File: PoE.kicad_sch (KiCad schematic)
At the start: 41 parts, among them J1001 8P8C_LED_Shielded_x2, J1002 8P8C_LED_Shielded_x2, U1001 7490220122, U1002 TCMT1107

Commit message: Still needs a lot of work
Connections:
- net POE0 renamed POE0_P
- net POE1 renamed POE0_N
- net POE2 renamed POE1_P
- net POE3 renamed POE1_N
- net POE4 renamed POE2_P
- net POE5 renamed POE2_N
- net POE6 renamed POE3_P
- net POE7 renamed POE3_N
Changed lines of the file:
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@@
 		)
 	)
-	(label "POE7"
+	(label "POE3_N"
 		(at 59.69 62.23 0)
 		(fields_autoplaced yes)
@@
 		)
 	)
-	(label "POE2"
+	(label "POE1_P"
 		(at 59.69 49.53 0)
 		(fields_autoplaced yes)
@@
 		)
 	)
-	(label "POE3"
+	(label "POE1_N"
 		(at 110.49 45.72 0)
 		(fields_autoplaced yes)
@@
 		)
 	)
-	(label "POE7"
+	(label "POE3_N"
 		(at 110.49 55.88 0)
 		(fields_autoplaced yes)
@@
 		)
 	)
-	(label "POE3"
+	(label "POE1_N"
 		(at 59.69 52.07 0)
 		(fields_autoplaced yes)
@@
 		)
 	)
-	(label "POE1"
+	(label "POE0_N"
 		(at 110.49 33.02 0)
 		(fields_autoplaced yes)
@@
 		)
 	)
-	(label "POE4"
+	(label "POE2_P"
 		(at 110.49 48.26 0)
 		(fields_autoplaced yes)
@@
 		)
 	)
-	(label "POE6"
+	(label "POE3_P"
 		(at 59.69 59.69 0)
 		(fields_autoplaced yes)
@@
 		)
 	)
-	(label "POE1"
+	(label "POE0_N"
 		(at 59.69 46.99 0)
 		(fields_autoplaced yes)
@@
 		)
 	)
-	(label "POE5"
+	(label "POE2_N"
 		(at 110.49 40.64 0)
 		(fields_autoplaced yes)
@@
 		)
 	)
-	(label "POE0"
+	(label "POE0_P"
 		(at 59.69 44.45 0)
 		(fields_autoplaced yes)
@@
 		)
 	)
-	(label "POE6"
+	(label "POE3_P"
 		(at 110.49 53.34 0)
 		(fields_autoplaced yes)
@@
 		)
 	)
-	(label "POE5"
+	(label "POE2_N"
 		(at 59.69 57.15 0)
 		(fields_autoplaced yes)
@@
 		)
 	)
-	(label "POE2"
+	(label "POE1_P"
 		(at 110.49 38.1 0)
 		(fields_autoplaced yes)
@@
 		)
 	)
-	(label "POE0"
+	(label "POE0_P"
 		(at 110.49 30.48 0)
 		(fields_autoplaced yes)
@@
 		)
 	)
-	(label "POE4"
+	(label "POE2_P"
 		(at 59.69 54.61 0)
 		(fields_autoplaced yes)
@@
 			)
 		)
+	)
+	(netclass_flag ""
+		(length 2.54)
+		(shape round)
+		(at 52.07 52.07 0)
+		(fields_autoplaced yes)
+		(effects
+			(font
+				(size 1.27 1.27)
+			)
+			(justify left bottom)
+		)
+		(property "Netclass" "Diff"
+			(at 52.7685 49.53 0)
+			(effects
+				(font
+					(size 1.27 1.27)
+					(italic yes)
+				)
+				(justify left)
+			)
+		)
+	)
+	(netclass_flag ""
+		(length 2.54)
+		(shape round)
+		(at 53.34 54.61 0)
+		(fields_autoplaced yes)
+		(effects
+			(font
+				(size 1.27 1.27)
+			)
+			(justify left bottom)
+		)
+		(property "Netclass" "Diff"
+			(at 54.0385 52.07 0)
+			(effects
+				(font
+					(size 1.27 1.27)
+					(italic yes)
+				)
+				(justify left)
+			)
+		)
+	)
+	(netclass_flag ""
+		(length 2.54)
+		(shape round)
+		(at 54.61 62.23 0)
+		(fields_autoplaced yes)
+		(effects
+			(font
+				(size 1.27 1.27)
+			)
+			(justify left bottom)
+		)
+		(property "Netclass" "Diff"
+			(at 55.3085 59.69 0)
+			(effects
+				(font
+					(size 1.27 1.27)
+					(italic yes)
+				)
+				(justify left)
+			)
+		)
+	)
+	(netclass_flag ""
+		(length 2.54)
+		(shape round)
+		(at 55.88 57.15 0)
+		(fields_autoplaced yes)
+		(effects
+			(font
+				(size 1.27 1.27)
+			)
+			(justify left bottom)
+		)
+		(property "Netclass" "Diff"
+			(at 56.5785 54.61 0)
+			(effects
+				(font
+					(size 1.27 1.27)
+					(italic yes)
+				)
+				(justify left)
+			)
+		)
+	)
+	(netclass_flag ""
+		(length 2.54)
+		(shape round)
+		(at 54.61 46.99 0)
+		(fields_autoplaced yes)
+		(effects
+			(font
+				(size 1.27 1.27)
+			)
+			(justify left bottom)
+		)
+		(property "Netclass" "Diff"
+			(at 55.3085 44.45 0)
+			(effects
+				(font
+					(size 1.27 1.27)
+					(italic yes)
+				)
+				(justify left)
+			)
+		)
+	)
+	(netclass_flag ""
+		(length 2.54)
+		(shape round)
+		(at 53.34 44.45 0)
+		(fields_autoplaced yes)
+		(effects
+			(font
+				(size 1.27 1.27)
+			)
+			(justify left bottom)
+		)
+		(property "Netclass" "Diff"
+			(at 54.0385 41.91 0)
+			(effects
+				(font
+					(size 1.27 1.27)
+					(italic yes)
+				)
+				(justify left)
+			)
+		)
+	)
+	(netclass_flag ""
+		(length 2.54)
+		(shape round)
+		(at 52.07 59.69 0)
+		(fields_autoplaced yes)
+		(effects
+			(font
+				(size 1.27 1.27)
+			)
+			(justify left bottom)
+		)
+		(property "Netclass" "Diff"
+			(at 52.7685 57.15 0)
+			(effects
+				(font
+					(size 1.27 1.27)
+					(italic yes)
+				)
+				(justify left)
+			)
+		)
+	)
+	(netclass_flag ""
+		(length 2.54)
+		(shape round)
+		(at 55.88 49.53 0)
+		(fields_autoplaced yes)
+		(effects
+			(font
+				(size 1.27 1.27)
+			)
+			(justify left bottom)
+		)
+		(property "Netclass" "Diff"
+			(at 56.5785 46.99 0)
+			(effects
+				(font
+					(size 1.27 1.27)
+					(italic yes)
+				)
+				(justify left)
+			)
+		)

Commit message: Added routing
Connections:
- net VDD_PRIME: now reaches C1007.1, D1001.1 (K), D1002.1 (K), D1003.1 (K), D1004.1 (K), FB1001.2
- net VSS_PRIME: now reaches C1007.2, D1006.2 (A), D1007.2 (A), D1008.2 (A), D1009.2 (A), FB1002.2
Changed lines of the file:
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@@
+		)
+	)
+	(label "VSS_PRIME"
+		(at 210.82 114.3 0)
+		(fields_autoplaced yes)
+		(effects
+			(font
+				(size 1.27 1.27)
+			)
+			(justify left bottom)
 		)
 	)
@@
 		(fields_autoplaced yes)
 		(effects
+			(font
+				(size 1.27 1.27)
+			)
+			(justify left bottom)
+		)
+	)
+	(label "VDD_PRIME"
+		(at 210.82 82.55 0)
+		(fields_autoplaced yes)
+		(effects

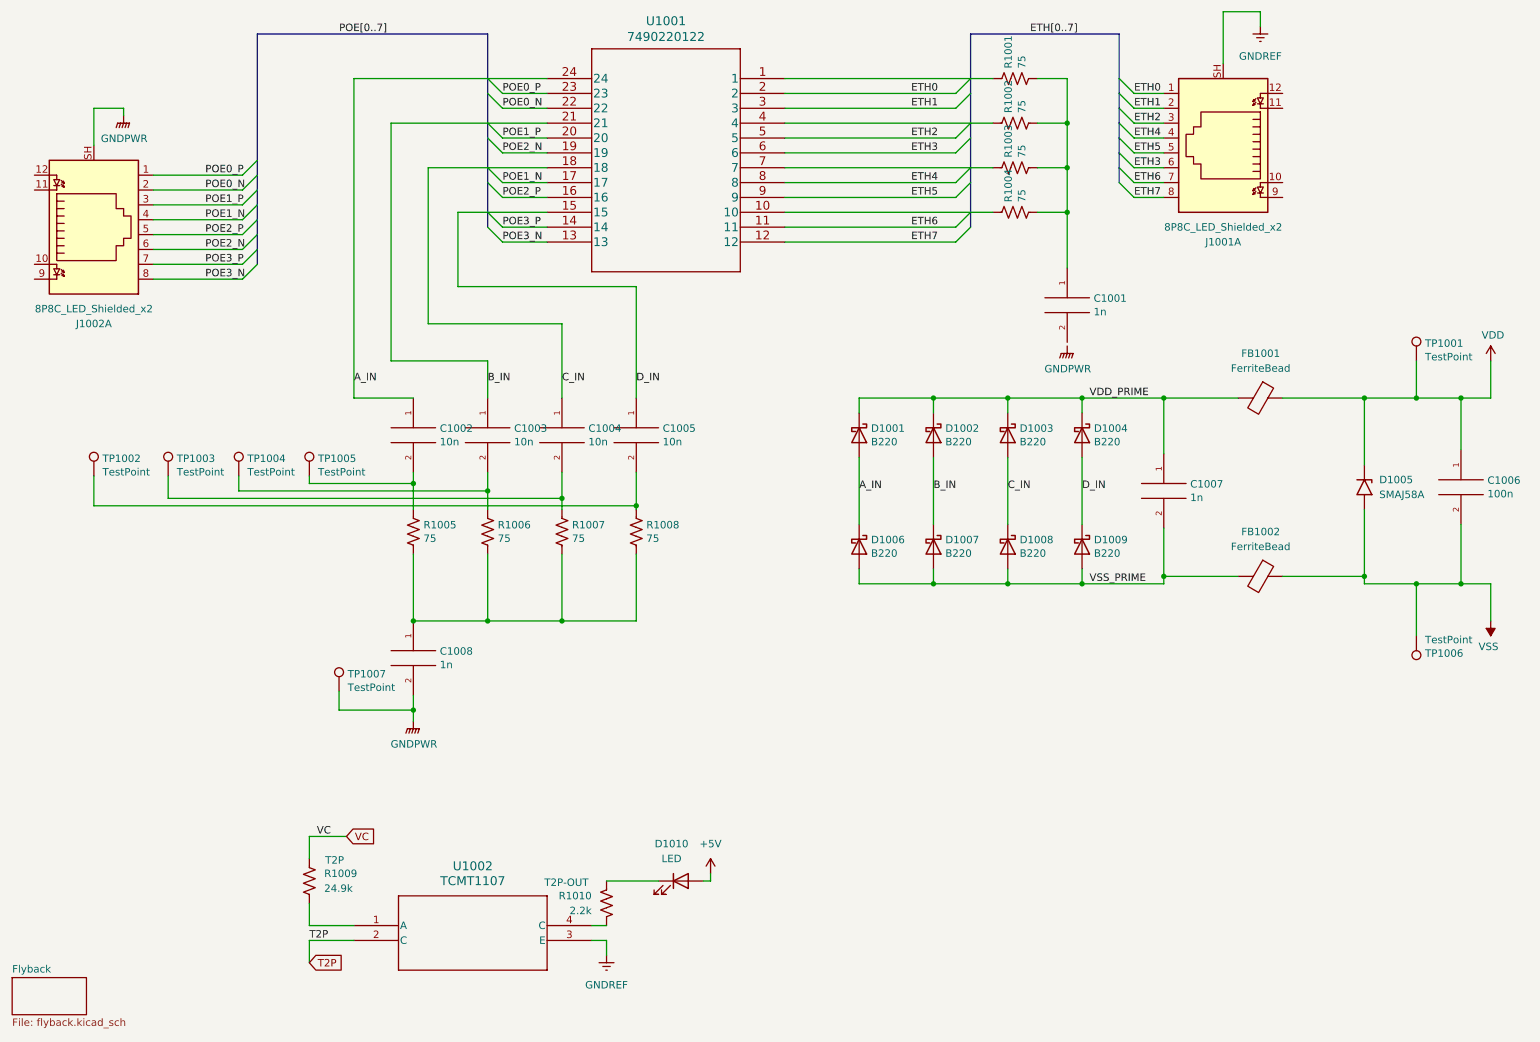
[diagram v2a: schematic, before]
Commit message: Changed main FET
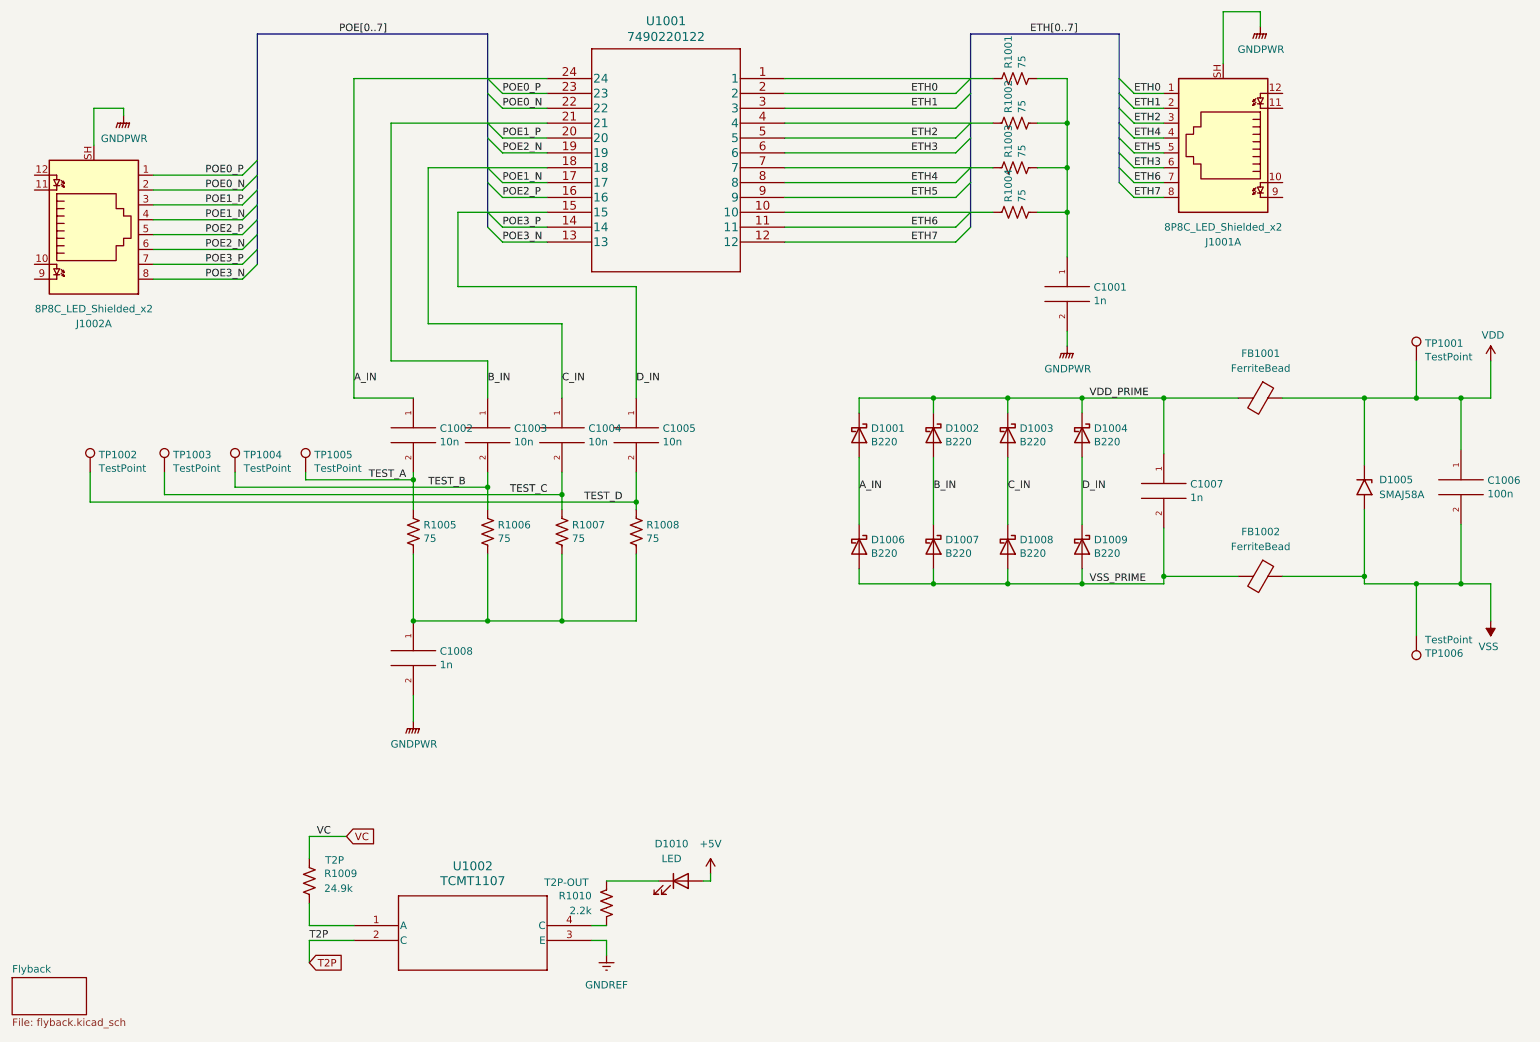
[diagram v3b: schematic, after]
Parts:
- removed TP1007: TestPoint, SparkFun-Connector:TestPoint-1.0mm, symbol Connector:TestPoint
- D1010: footprint LED_SMD:LED_0402_1005Metric -> LED_SMD:LED_0805_2012Metric
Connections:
- net GNDPWR: now also C1001.2, J1001.SH
- net GNDREF: no longer J1001.SH
- net TEST_A: now reaches C1002.2, R1005.1, TP1005.1
- net TEST_B: now reaches C1003.2, R1006.1, TP1004.1
- net TEST_C: now reaches C1004.2, R1007.1, TP1003.1
- net TEST_D: now reaches C1005.2, R1008.1, TP1002.1
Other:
- moved on the sheet: C1001, TP1002, TP1003, TP1004, TP1005

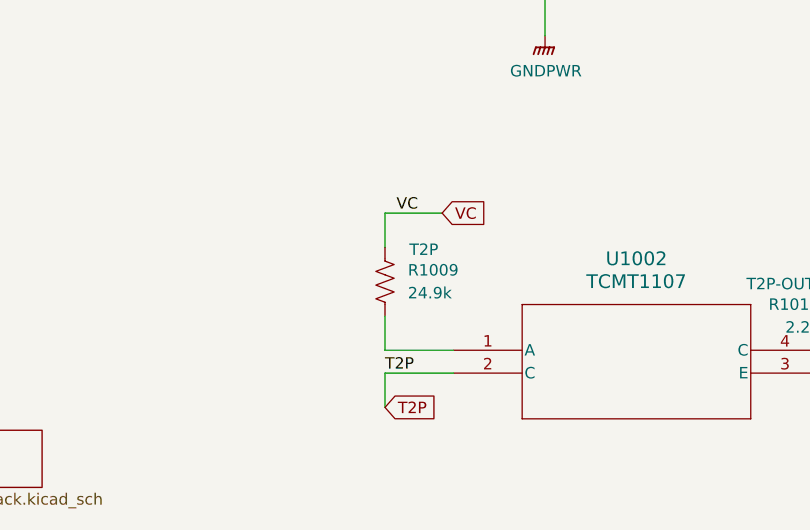
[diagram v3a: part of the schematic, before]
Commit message: Added more routing
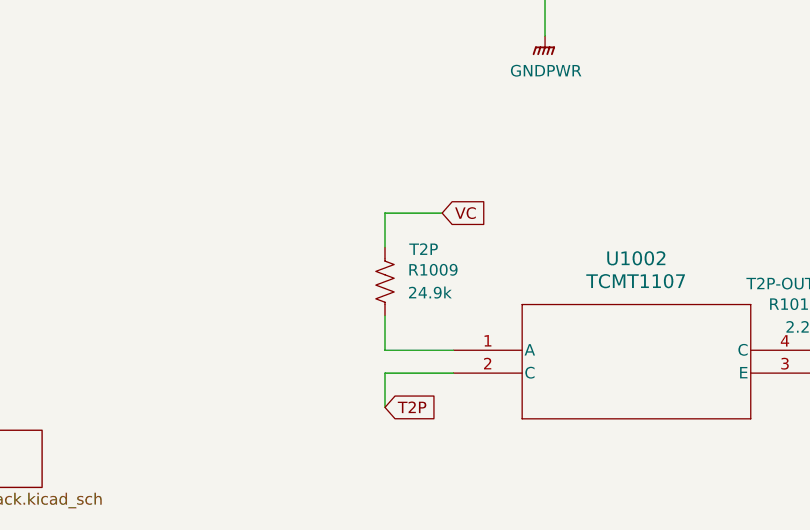
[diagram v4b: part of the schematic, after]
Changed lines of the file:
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@@
-		)
-	)
-	(label "VC"
-		(at 78.74 157.48 0)
-		(fields_autoplaced yes)
-		(effects
-			(font
-				(size 1.27 1.27)
-			)
-			(justify left bottom)
 		)
 	)
@@
 		(fields_autoplaced yes)
 		(effects
-			(font
-				(size 1.27 1.27)
-			)
-			(justify left bottom)
-		)
-	)
-	(label "T2P"
-		(at 77.47 175.26 0)
-		(fields_autoplaced yes)
-		(effects

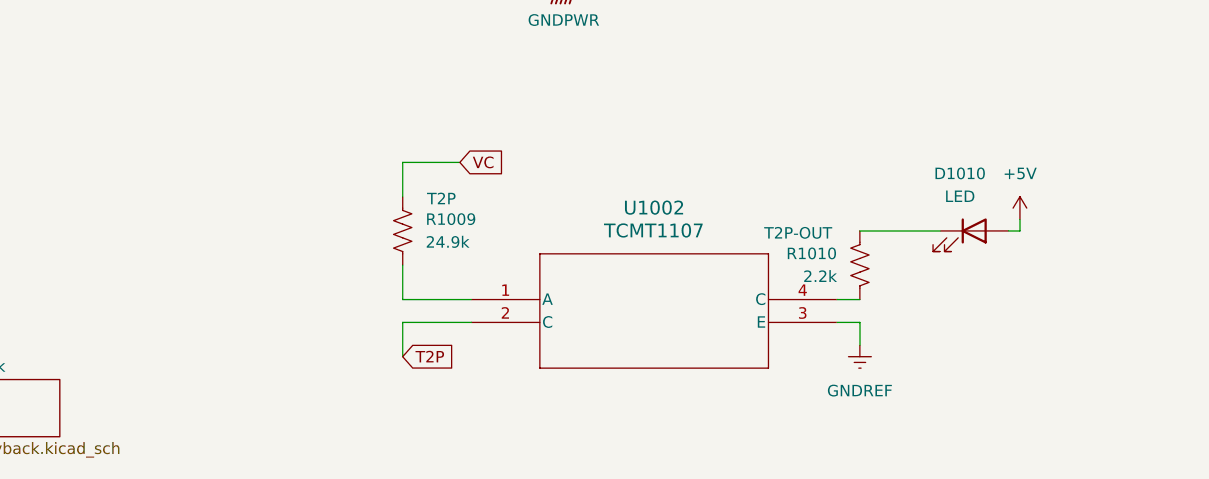
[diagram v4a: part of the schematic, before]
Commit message: Added buck
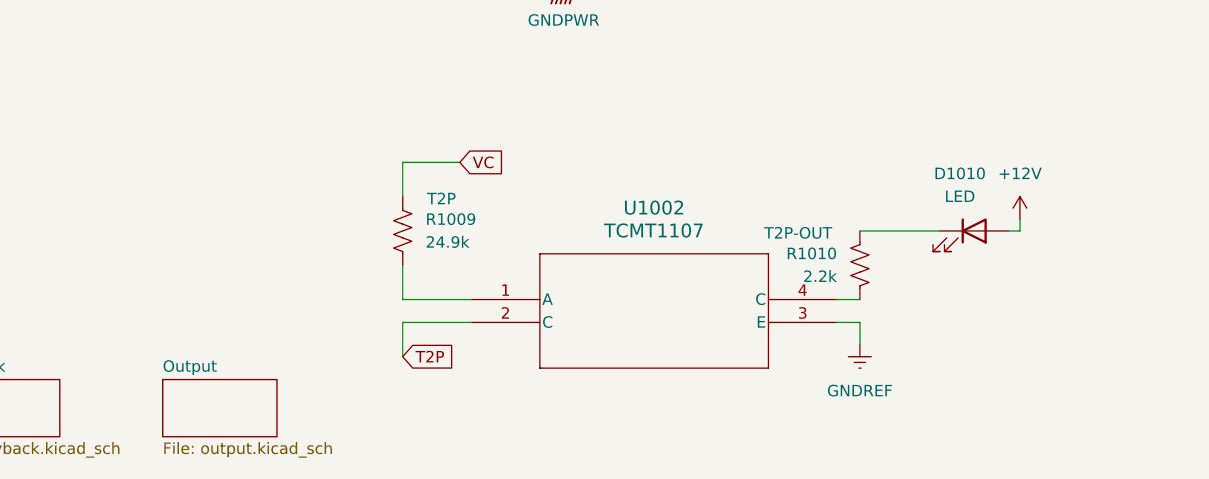
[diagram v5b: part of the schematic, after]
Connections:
- net +5V renamed +12V
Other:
- added sheet Output (output.kicad_sch)
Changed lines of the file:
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@@
+	)
+	(symbol
+		(lib_id "power:+12V")
+		(at 146.05 163.83 0)
+		(unit 1)
+		(exclude_from_sim no)
+		(in_bom yes)
+		(on_board yes)
+		(dnp no)
+		(fields_autoplaced yes)
+		(property "Reference" "#PWR014"
+			(at 146.05 167.64 0)
+			(effects
+				(font
+					(size 1.27 1.27)
+				)
+				(hide yes)
+			)
+		)
+		(property "Value" "+12V"
+			(at 146.05 158.75 0)
+			(effects
+				(font
+					(size 1.27 1.27)
+				)
+			)
+		)
+		(property "Footprint" ""
+			(at 146.05 163.83 0)
+			(effects
+				(font
+					(size 1.27 1.27)
+				)
+				(hide yes)
+			)
+		)
+		(property "Datasheet" ""
+			(at 146.05 163.83 0)
+			(effects
+				(font
+					(size 1.27 1.27)
+				)
+				(hide yes)
+			)
+		)
+		(property "Description" "Power symbol creates a global label with name \"+12V\""
+			(at 146.05 163.83 0)
+			(effects
+				(font
+					(size 1.27 1.27)
+				)
+				(hide yes)
+			)
+		)
+		(pin "1"
+		)
+		(instances
+			(project "PoE"
+				(path "/e8d70991-5081-4afb-b8c3-5ce9f62355e0"
+					(reference "#PWR014")
+					(unit 1)
+				)
+			)
+		)
 	)
 	(symbol
@@
 				(path "/e8d70991-5081-4afb-b8c3-5ce9f62355e0"
 					(reference "D1005")
-					(unit 1)
-				)
-			)
-		)
-	)
-	(symbol
-		(lib_id "power:+5V")
-		(at 146.05 163.83 0)
-		(unit 1)
-		(exclude_from_sim no)
-		(in_bom yes)
-		(on_board yes)
-		(dnp no)
-		(property "Reference" "#PWR01007"
-			(at 146.05 167.64 0)
-			(effects
-				(font
-					(size 1.27 1.27)
-				)
-				(hide yes)
-			)
-		)
-		(property "Value" "+5V"
-			(at 146.05 158.75 0)
-			(effects
-				(font
-					(size 1.27 1.27)
-				)
-			)
-		)
-		(property "Footprint" ""
-			(at 146.05 163.83 0)
-			(effects
-				(font
-					(size 1.27 1.27)
-				)
-				(hide yes)
-			)
-		)
-		(property "Datasheet" ""
-			(at 146.05 163.83 0)
-			(effects
-				(font
-					(size 1.27 1.27)
-				)
-				(hide yes)
-			)
-		)
-		(property "Description" "Power symbol creates a global label with name \"+5V\""
-			(at 146.05 163.83 0)
-			(effects
-				(font
-					(size 1.27 1.27)
-				)
-				(hide yes)
-			)
-		)
-		(pin "1"
-		)
-		(instances
-			(project "PoE"
-				(path "/e8d70991-5081-4afb-b8c3-5ce9f62355e0"
-					(reference "#PWR01007")
 					(unit 1)
 				)
@@
 				)
 			)
+		)
+	)
+	(sheet
+		(at 50.8 181.61)
+		(size 12.7 6.35)
+		(fields_autoplaced yes)
+		(stroke
+			(width 0.1524)
+			(type solid)
+		)
+		(fill
+			(color 0 0 0 0.0000)
+		)
+		(property "Sheetname" "Output"
+			(at 50.8 180.8984 0)
+			(effects
+				(font
+					(size 1.27 1.27)
+				)
+				(justify left bottom)
+			)
+		)
+		(property "Sheetfile" "output.kicad_sch"
+			(at 50.8 188.5446 0)
+			(effects
+				(font
+					(size 1.27 1.27)
+				)
+				(justify left top)
+			)
+		)
+		(instances
+			(project "PoE"
+				(path "/e8d70991-5081-4afb-b8c3-5ce9f62355e0"
+					(page "3")
+				)
+			)

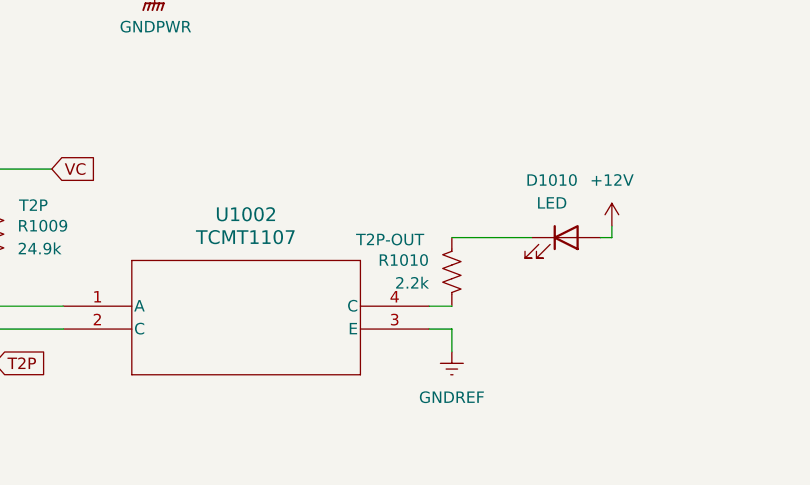
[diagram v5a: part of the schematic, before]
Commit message: Added LEDs for status
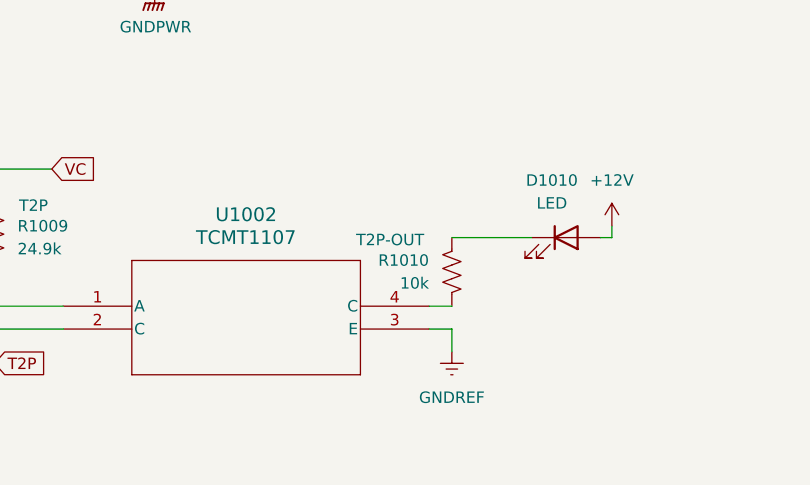
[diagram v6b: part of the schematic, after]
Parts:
- R1010: value 2.2k -> 10k
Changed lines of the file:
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@@
 			)
 		)
-		(property "Value" "2.2k"
+		(property "Value" "10k"
 			(at 125.73 170.1799 0)
 			(effects
